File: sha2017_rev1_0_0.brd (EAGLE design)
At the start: 95 x 86 mm, 201 parts, among them IC1 CP210X_USB_UART, IC2 AP7215, IC3 ESP32WROOM32, IC4 TP4056, M1 MOTOR10MM, Q3 MMBT2222A, Q4 MMBT2222A, Q5 SI1304 BDL, T4 AO3400, T5 AO3400, T6 AO3400, U1 MPR121QR2, X2 2908-05WB-MG, X4 JST-PH3

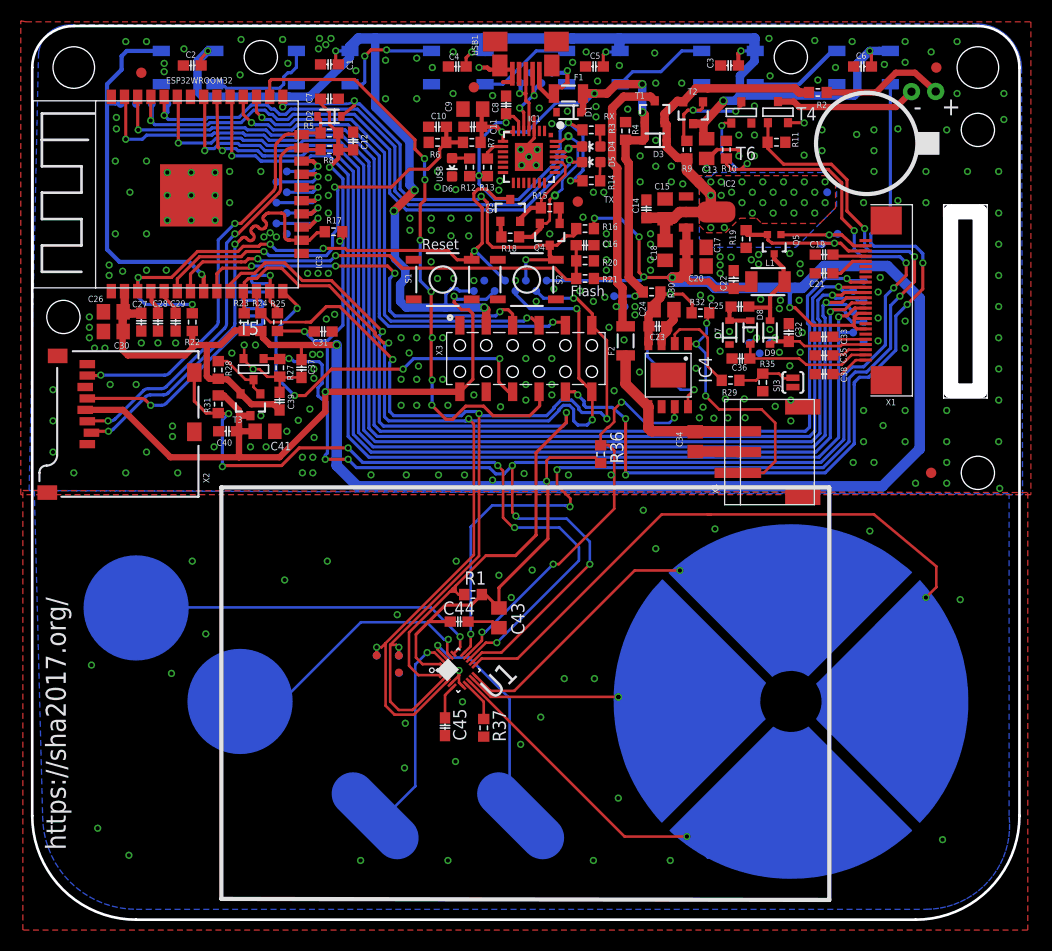
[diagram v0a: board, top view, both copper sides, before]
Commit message: Removed unnecessary MOSFETs
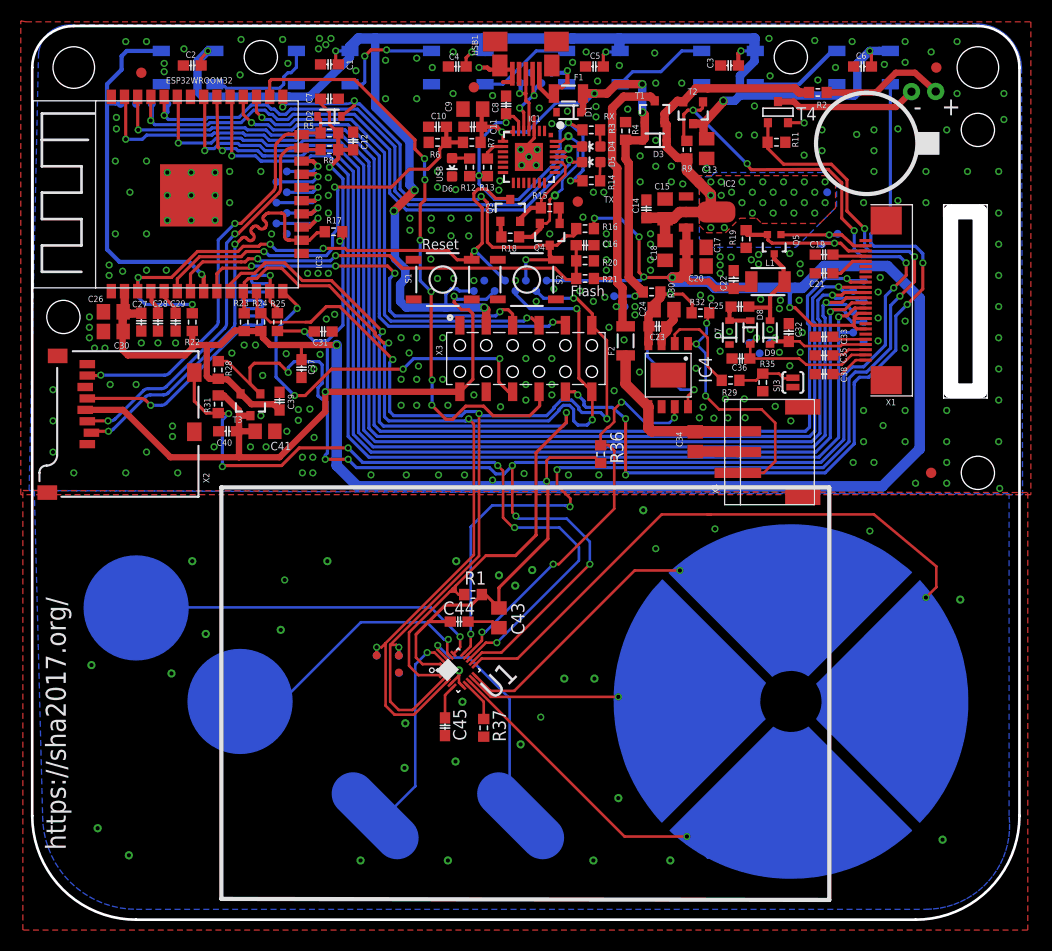
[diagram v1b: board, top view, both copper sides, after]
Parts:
- removed R10: 10k, 00ralf:R0603-DASHES
- removed R27: 100k, 00ralf:R0603-DASHES
- removed T5, T6: AO3400, zetex:SOT-23
- R28, R4, R9: value 10k -> 100k
- moved $$U$3 11.3 mm to (23.9, 26.9)
- moved $$U$1 1.20 mm to (46.5, 31.1)
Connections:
- removed net N$17: R28.1, T3.1, T5.1
- removed net N$53: R9.1, T2.1, T6.1
- net GND: no longer R10.2, R27.1, T5.2, T6.2
- net PERIPHERAL_POWER_EN: now also R28.1, R9.1, T2.1, T3.1; no longer R10.1, R27.2, T5.3, T6.3
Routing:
- net PERIPHERAL_POWER_EN: track 151.0 -> 164.6 mm
- net GND: track 37.5 -> 24.4 mm, vias 294 -> 288
- net N$53: track 10.9 -> 0.00 mm, vias 2 -> 0
- net N$17: track 5.77 -> 0.00 mm
- net N$56: track 18.4 -> 20.0 mm, vias 2 -> 1

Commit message: Finalized LED and SD card power switches, rerouted
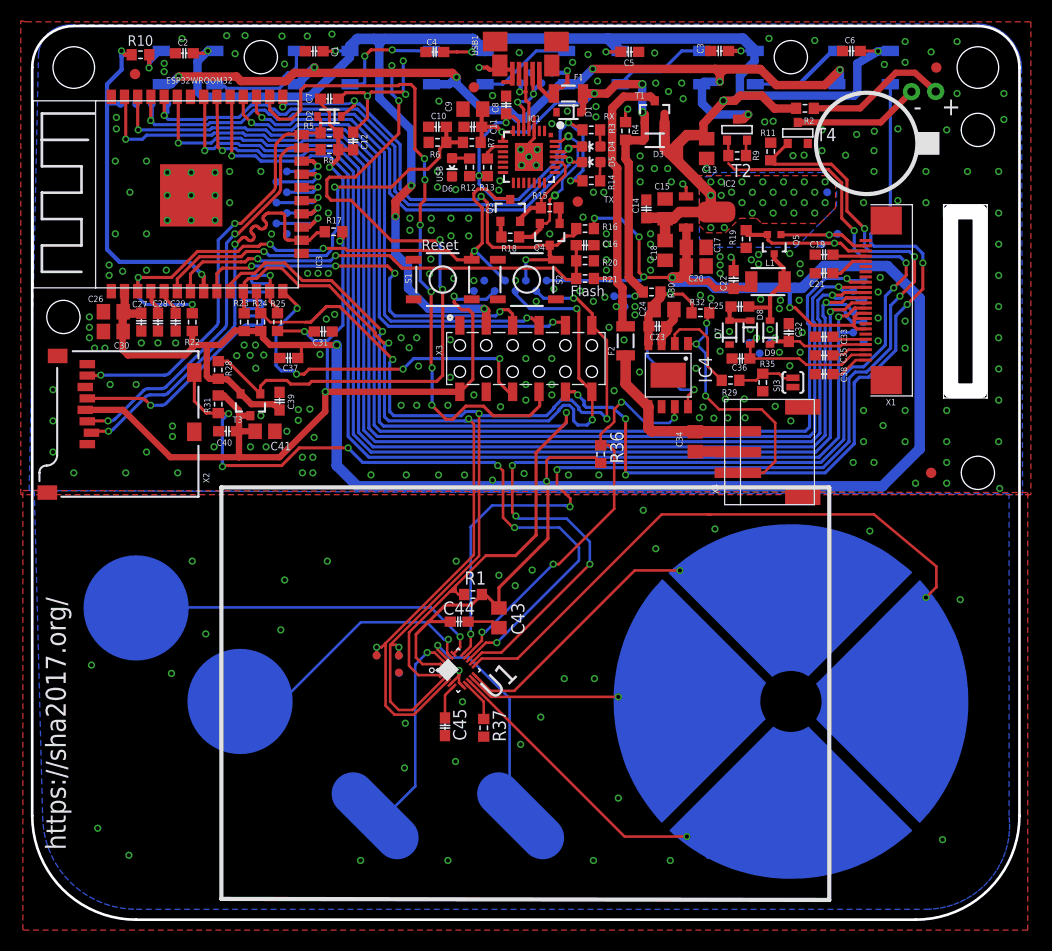
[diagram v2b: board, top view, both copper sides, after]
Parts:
- added R10: 470, 00ralf:R0603-DASHES
- T2: value (none) -> AO3400; device SparkFun-DiscreteSemi:SOT23-3 -> zetex:SOT-23
- moved R9 4.87 mm to (67.8, 72.5), turned to 0 degrees
- moved T2 4.57 mm to (67.8, 75.0)
- moved C5 3.68 mm to (57.5, 82.5), turned to 180 degrees
- moved T4 2.76 mm to (73.7, 74.7)
- moved C4 2.57 mm to (38.7, 82.5)
- moved R2 1.96 mm to (74.4, 77.1)
- moved C1 1.94 mm to (27.1, 82.6)
- moved C6 1.84 mm to (78.8, 82.6)
- moved C3 1.69 mm to (66.1, 82.6)
- moved C37 1.59 mm to (24.7, 53.0), turned to 180 degrees
- moved C2 1.40 mm to (14.6, 82.4)
- moved R11 1.05 mm to (71.1, 72.9), turned to 90 degrees
- moved FD2 0.62 mm to (9.90, 80.4)
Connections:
- new net N$15: D105.4, R10.1
- new net SD_POWER_EN: D100.3, D101.3, D102.3, D103.3, D104.3, D105.3, R28.1, T2.1, T3.1
- net GND: now also R9.2, T2.2; no longer D100.3, D101.3, D102.3, D103.3, D104.3, D105.3
- net PERIPHERAL_POWER_EN: now also T2.3; no longer R28.1, T2.1, T3.1
- net VCC: now also C1.2, C13.1, C2.2, C3.2, C4.2, C5.2, C6.2, D100.1, D101.1, D102.1, D103.1, D104.1, D105.1, X3.2; no longer R9.2, T2.2
- net WS2812_DATA: now also R10.2; no longer D105.4
- net WS2812_POWER: no longer C1.2, C13.1, C2.2, C3.2, C4.2, C5.2, C6.2, D100.1, D101.1, D102.1, D103.1, D104.1, D105.1, T2.3, X3.2
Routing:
- net SD_POWER_EN: track 0.00 -> 162.1 mm, vias 0 -> 11
- net WS2812_POWER: track 155.3 -> 0.00 mm, vias 10 -> 0
- net VCC: track 38.7 -> 184.6 mm, vias 25 -> 35
- net PERIPHERAL_POWER_EN: track 164.6 -> 109.3 mm, vias 11 -> 6
- net GND: track 24.4 -> 43.3 mm, vias 288 -> 274
- net EXTIO-3: track 58.2 -> 63.4 mm
- net N$15: track 0.00 -> 3.44 mm, vias 0 -> 1
- net EXTIO-4: track 37.4 -> 35.1 mm
- net WS2812_DATA: track 36.3 -> 34.4 mm, vias 1 -> 2
- net N$18: track 12.0 -> 13.8 mm
- net N$16: track 13.7 -> 12.2 mm
- net VIBRATOR: track 101.5 -> 100.6 mm
